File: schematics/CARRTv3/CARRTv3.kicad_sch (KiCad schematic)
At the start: 28 parts, among them J1 LCD_with_5_Buttons, M1 Rear Right, M2 Front Right, M3 Front Left, M4 Rear Left, M5 Lidar Servo, P1 PowerBoost_1000C, SW1 Switch, SW2 RPi0 Shutdown, SW3 Right Encoder, SW4 Left Encoder, SW5 Switch, T1 2N2222, U1 BNO055, X1 Raspberry_Pi_Zero2, X2 Raspberry_Pico2

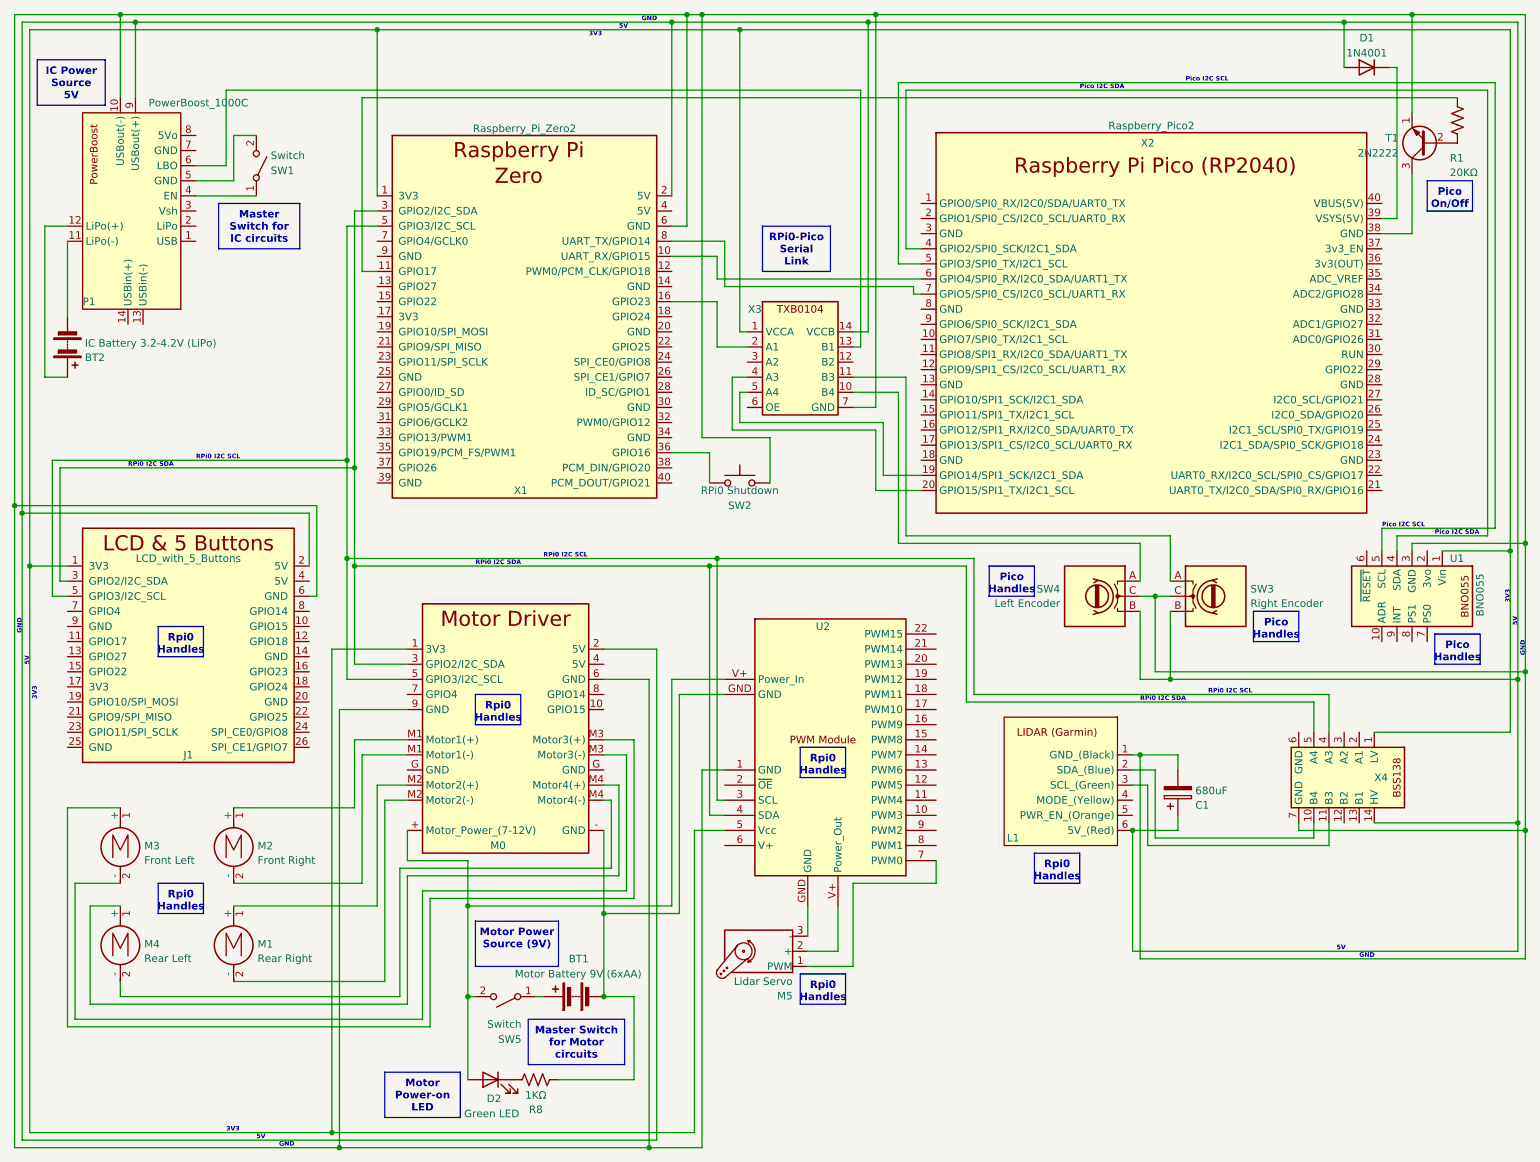
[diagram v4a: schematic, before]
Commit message: Add buzzer, missing OE & GND wires, clean up wiring
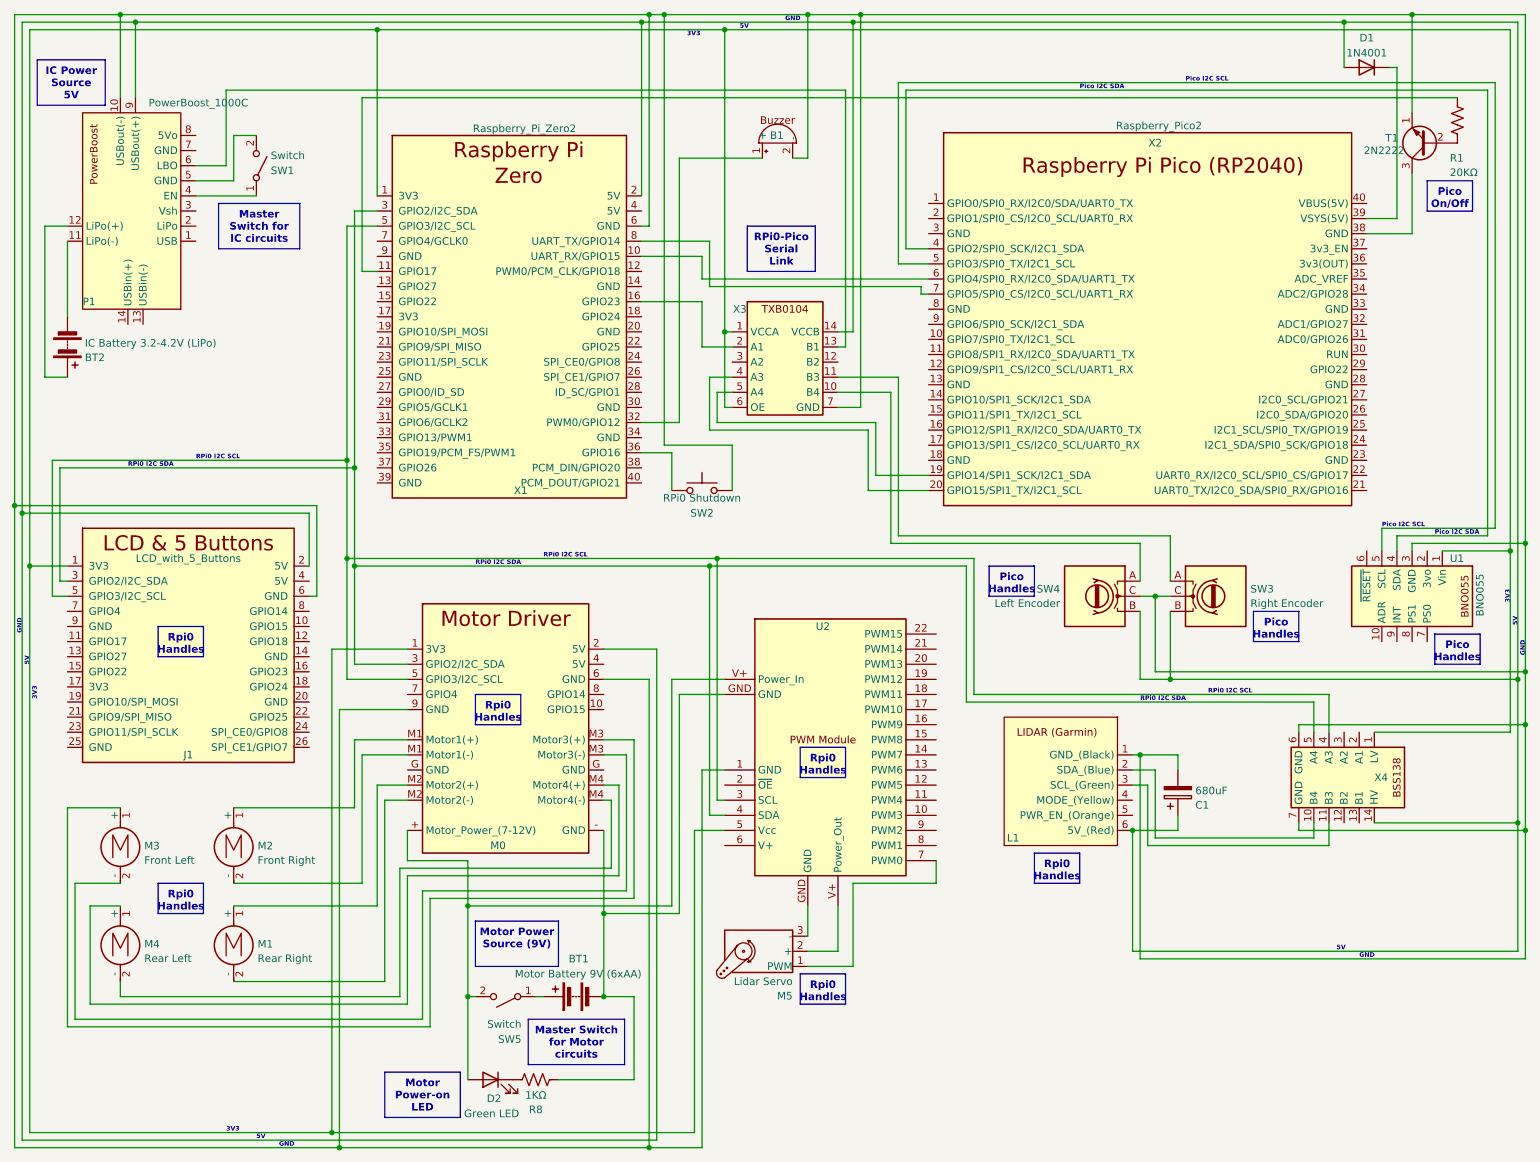
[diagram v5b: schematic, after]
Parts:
- added B1: ~, symbol CARRTv3:Buzzer
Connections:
- net at J1.1 (3V3), M0.1 (3V3), U1.1 (Vin)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: now also X3.6 (OE)
- net at X4.6 (GND): now also C1.2, J1.6 (GND), L1.1 (GND_(Black)), M0.6 (GND), M0.9 (GND), P1.10 (USBout(-)), SW2.1, SW3.C, SW4.C, T1.1 (E), U1.3 (GND), U2.1 (GND), X1.6 (GND), X3.7 (GND), X4.7 (GND), B1.2 (-)
- net at X1.32 (PWM0/GPIO12): now also B1.1 (+)
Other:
- moved on the sheet: SW2, X1, X2, X3

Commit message: Update to exact pins being used; update colors of wires to actual; cosmetic repositionings
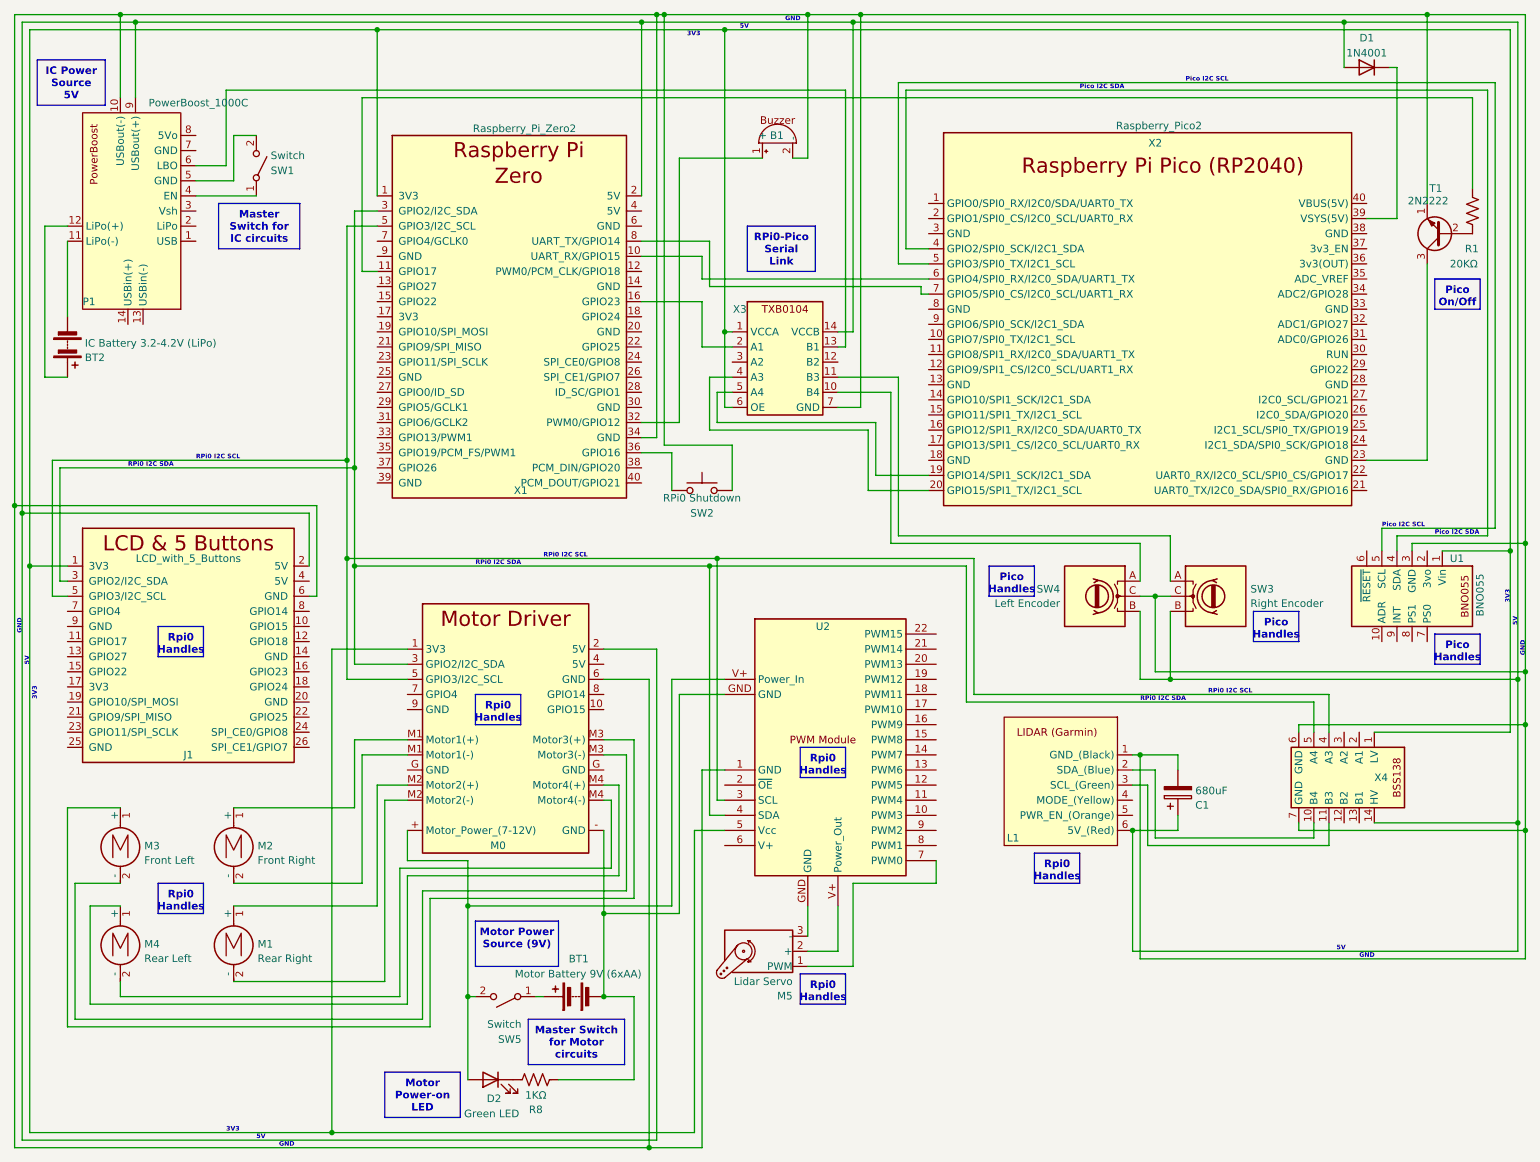
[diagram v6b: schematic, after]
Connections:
- net at B1.2 (-), C1.2, J1.6 (GND)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: now also X1.34 (GND); no longer M0.9 (GND), X1.6 (GND)
- net at T1.3 (C): now also X2.23 (GND); no longer X2.38 (GND)
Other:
- moved on the sheet: R1, T1
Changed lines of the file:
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@@
   (junction (at 264.16 102.87) (diameter 0) (color 204 102 0 1)
   )
+  (junction (at 250.19 12.7) (diameter 0) (color 0 0 0 1)
+  )
   (junction (at 265.43 148.59) (diameter 0) (color 194 0 0 1)
   )
@@
   (junction (at 73.66 15.24) (diameter 0) (color 204 102 0 1)
   )
-  (junction (at 119.38 12.7) (diameter 0) (color 0 0 0 1)
-  )
   (junction (at 12.7 95.25) (diameter 0) (color 0 0 0 1)
   )
   (junction (at 13.97 96.52) (diameter 0) (color 194 0 0 1)
   )
+  (junction (at 120.65 12.7) (diameter 0) (color 0 0 0 1)
+  )
   (junction (at 111.76 163.83) (diameter 0) (color 0 0 0 1)
   )
@@
   (junction (at 129.54 105.41) (diameter 0) (color 0 0 132 1)
   )
-  (junction (at 67.31 203.2) (diameter 0) (color 0 0 0 1)
-  )
   (junction (at 204.47 110.49) (diameter 0) (color 0 0 0 1)
   )
   (junction (at 130.81 104.14) (diameter 0) (color 194 194 0 1)
-  )
-  (junction (at 247.65 12.7) (diameter 0) (color 0 0 0 1)
   )
   (junction (at 88.9 177.8) (diameter 0) (color 132 0 0 1)
@@
     (stroke (width 0) (type default) (color 0 0 132 1))
   )
-  (wire (pts (xy 119.38 12.7) (xy 119.38 48.26))
-    (stroke (width 0) (type default) (color 0 0 0 1))
-  )
   (wire (pts (xy 128.27 68.58) (xy 128.27 60.96))
     (stroke (width 0) (type default))
@@
   )
   (wire (pts (xy 123.19 86.36) (xy 123.19 92.71))
-    (stroke (width 0) (type default))
+    (stroke (width 0) (type default) (color 128 77 0 1))
   )
   (wire (pts (xy 33.02 13.97) (xy 118.11 13.97))
@@
   )
   (wire (pts (xy 43.18 43.18) (xy 53.34 43.18))
-    (stroke (width 0) (type default))
+    (stroke (width 0) (type default) (color 194 194 194 1))
   )
   (wire (pts (xy 133.35 66.04) (xy 132.08 66.04))
@@
     (stroke (width 0) (type default) (color 204 102 0 1))
   )
-  (wire (pts (xy 240.03 49.53) (xy 247.65 49.53))
-    (stroke (width 0) (type default) (color 0 0 0 1))
-  )
   (wire (pts (xy 49.53 162.56) (xy 73.66 162.56))
     (stroke (width 0.2286) (type default) (color 132 0 0 1))
-  )
-  (wire (pts (xy 67.31 203.2) (xy 12.7 203.2))
-    (stroke (width 0) (type default) (color 0 0 0 1))
   )
   (wire (pts (xy 124.46 36.83) (xy 138.43 36.83))
@@
     (stroke (width 0) (type default) (color 194 0 0 1))
   )
-  (wire (pts (xy 247.65 12.7) (xy 247.65 29.21))
+  (wire (pts (xy 250.19 12.7) (xy 250.19 44.45))
     (stroke (width 0) (type default) (color 0 0 0 1))
   )
@@
   (wire (pts (xy 266.7 149.86) (xy 266.7 171.45))
     (stroke (width 0) (type default) (color 0 0 0 1))
+  )
+  (wire (pts (xy 71.12 26.67) (xy 257.81 26.67))
+    (stroke (width 0) (type default))
   )
   (wire (pts (xy 118.11 81.28) (xy 124.46 81.28))
@@
     (stroke (width 0) (type default) (color 0 0 132 1))
   )
+  (wire (pts (xy 118.11 83.82) (xy 120.65 83.82))
+    (stroke (width 0) (type default) (color 0 0 0 1))
+  )
   (wire (pts (xy 132.08 127) (xy 124.46 127))
     (stroke (width 0.2286) (type default) (color 0 0 0 1))
   )
+  (wire (pts (xy 120.65 83.82) (xy 120.65 12.7))
+    (stroke (width 0) (type default) (color 0 0 0 1))
+  )
   (wire (pts (xy 68.58 87.63) (xy 19.05 87.63))
     (stroke (width 0) (type default) (color 194 194 0 1))
@@
   )
   (wire (pts (xy 123.19 86.36) (xy 118.11 86.36))
-    (stroke (width 0) (type default))
+    (stroke (width 0) (type default) (color 128 77 0 1))
   )
   (wire (pts (xy 73.66 142.24) (xy 78.74 142.24))
@@
     (stroke (width 0.2286) (type default) (color 72 0 0 1))
   )
+  (wire (pts (xy 257.81 26.67) (xy 257.81 41.91))
+    (stroke (width 0) (type default))
+  )
   (wire (pts (xy 30.48 177.8) (xy 30.48 175.26))
     (stroke (width 0.2286) (type default) (color 72 0 0 1))
@@
   (wire (pts (xy 204.47 139.7) (xy 204.47 151.13))
     (stroke (width 0) (type default) (color 0 0 132 1))
-  )
-  (wire (pts (xy 154.94 12.7) (xy 247.65 12.7))
-    (stroke (width 0) (type default) (color 0 0 0 1))
   )
   (wire (pts (xy 161.29 100.33) (xy 207.01 100.33))
@@
     (stroke (width 0.2286) (type default) (color 132 0 0 1))
   )
+  (wire (pts (xy 154.94 12.7) (xy 250.19 12.7))
+    (stroke (width 0) (type default) (color 0 0 0 1))
+  )
   (wire (pts (xy 152.4 68.58) (xy 152.4 25.4))
     (stroke (width 0) (type default))
@@
     (stroke (width 0) (type default) (color 194 0 0 1))
   )
-  (wire (pts (xy 78.74 129.54) (xy 67.31 129.54))
-    (stroke (width 0) (type default) (color 0 0 0 1))
-  )
   (wire (pts (xy 118.11 60.96) (xy 128.27 60.96))
     (stroke (width 0) (type default))
@@
     (stroke (width 0) (type default) (color 194 194 0 1))
   )
-  (wire (pts (xy 266.7 12.7) (xy 247.65 12.7))
+  (wire (pts (xy 266.7 12.7) (xy 250.19 12.7))
     (stroke (width 0) (type default) (color 0 0 0 1))
   )
   (wire (pts (xy 77.47 177.8) (xy 30.48 177.8))
     (stroke (width 0.2286) (type default) (color 72 0 0 1))
-  )
-  (wire (pts (xy 67.31 129.54) (xy 67.31 203.2))
-    (stroke (width 0) (type default) (color 0 0 0 1))
   )
   (wire (pts (xy 241.3 148.59) (xy 265.43 148.59))
@@
     (stroke (width 0) (type default))
   )
-  (wire (pts (xy 119.38 12.7) (xy 121.92 12.7))
+  (wire (pts (xy 30.48 12.7) (xy 120.65 12.7))
     (stroke (width 0) (type default) (color 0 0 0 1))
   )
@@
     (stroke (width 0) (type default))
   )
-  (wire (pts (xy 67.31 203.2) (xy 119.38 203.2))
+  (wire (pts (xy 12.7 203.2) (xy 119.38 203.2))
     (stroke (width 0) (type default) (color 0 0 0 1))
   )
@@
     (stroke (width 0) (type default))
   )
+  (wire (pts (xy 120.65 12.7) (xy 121.92 12.7))
+    (stroke (width 0) (type default) (color 0 0 0 1))
+  )
   (wire (pts (xy 266.7 12.7) (xy 266.7 101.6))
     (stroke (width 0) (type default) (color 0 0 0 1))
@@
   (wire (pts (xy 121.92 12.7) (xy 146.05 12.7))
     (stroke (width 0) (type default) (color 0 0 0 1))
-  )
-  (wire (pts (xy 71.12 26.67) (xy 255.27 26.67))
-    (stroke (width 0) (type default))
   )
   (wire (pts (xy 118.11 13.97) (xy 118.11 43.18))
@@
     (stroke (width 0) (type default))
   )
-  (wire (pts (xy 118.11 48.26) (xy 119.38 48.26))
-    (stroke (width 0) (type default) (color 0 0 0 1))
-  )
   (wire (pts (xy 21.59 146.05) (xy 30.48 146.05))
     (stroke (width 0.2286) (type default) (color 132 0 0 1))
@@
     (stroke (width 0) (type default))
   )
-  (wire (pts (xy 30.48 12.7) (xy 119.38 12.7))
+  (wire (pts (xy 250.19 87.63) (xy 240.03 87.63))
     (stroke (width 0) (type default) (color 0 0 0 1))
   )
@@
     (stroke (width 0) (type default) (color 0 0 132 1))
   )
-  (wire (pts (xy 247.65 39.37) (xy 247.65 49.53))
+  (wire (pts (xy 250.19 54.61) (xy 250.19 87.63))
     (stroke (width 0) (type default) (color 0 0 0 1))
   )
@@
   )
   (text_box "Pico On/Off"
-    (at 250.19 40.64 0) (size 7.62 5.08)
+    (at 251.46 57.15 0) (size 7.62 5.08)
     (stroke (width 0) (type default))
     (fill (type none))
@@
     )
   )
-  (symbol (lib_id "Transistor_BJT:2N2219") (at 250.19 34.29 180) (unit 1)
+  (symbol (lib_id "Transistor_BJT:2N2219") (at 252.73 49.53 180) (unit 1)
     (in_bom yes) (on_board yes) (dnp no)
-    (property "Reference" "T1" (at 245.3387 33.4553 0)
+    (property "Reference" "T1" (at 252.73 41.91 0)
       (effects (font (size 1.27 1.27)) (justify left))
     )
-    (property "Value" "2N2222" (at 246.38 35.56 0)
+    (property "Value" "2N2222" (at 253.7713 44.0147 0)
       (effects (font (size 1.27 1.27)) (justify left))
     )
-    (property "Footprint" "Package_TO_SOT_THT:TO-39-3" (at 245.11 32.385 0)
+    (property "Footprint" "Package_TO_SOT_THT:TO-39-3" (at 247.65 47.625 0)
       (effects (font (size 1.27 1.27) italic) (justify left) hide)
     )
-    (property "Datasheet" "http://www.onsemi.com/pub_link/Collateral/2N2219-D.PDF" (at 250.19 34.29 0)
+    (property "Datasheet" "http://www.onsemi.com/pub_link/Collateral/2N2219-D.PDF" (at 252.73 49.53 0)
       (effects (font (size 1.27 1.27)) (justify left) hide)
     )
@@
     )
   )
-  (symbol (lib_id "Device:R_US") (at 255.27 30.48 0) (unit 1)
+  (symbol (lib_id "Device:R_US") (at 257.81 45.72 0) (unit 1)
     (in_bom yes) (on_board yes) (dnp no)
-    (property "Reference" "R1" (at 254 36.83 0)
+    (property "Reference" "R1" (at 256.54 52.07 0)
       (effects (font (size 1.27 1.27)) (justify left))
     )
-    (property "Value" "20KΩ" (at 254 39.2542 0)
+    (property "Value" "20KΩ" (at 254 54.61 0)
       (effects (font (size 1.27 1.27)) (justify left))
     )
-    (property "Footprint" "" (at 256.286 30.734 90)
+    (property "Footprint" "" (at 258.826 45.974 90)
       (effects (font (size 1.27 1.27)) hide)
     )
-    (property "Datasheet" "~" (at 255.27 30.48 0)
+    (property "Datasheet" "~" (at 257.81 45.72 0)
       (effects (font (size 1.27 1.27)) hide)
     )
